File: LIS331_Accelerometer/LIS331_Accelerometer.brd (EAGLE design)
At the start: 39.3 x 26.4 mm, 8 parts, among them U1 LIS331

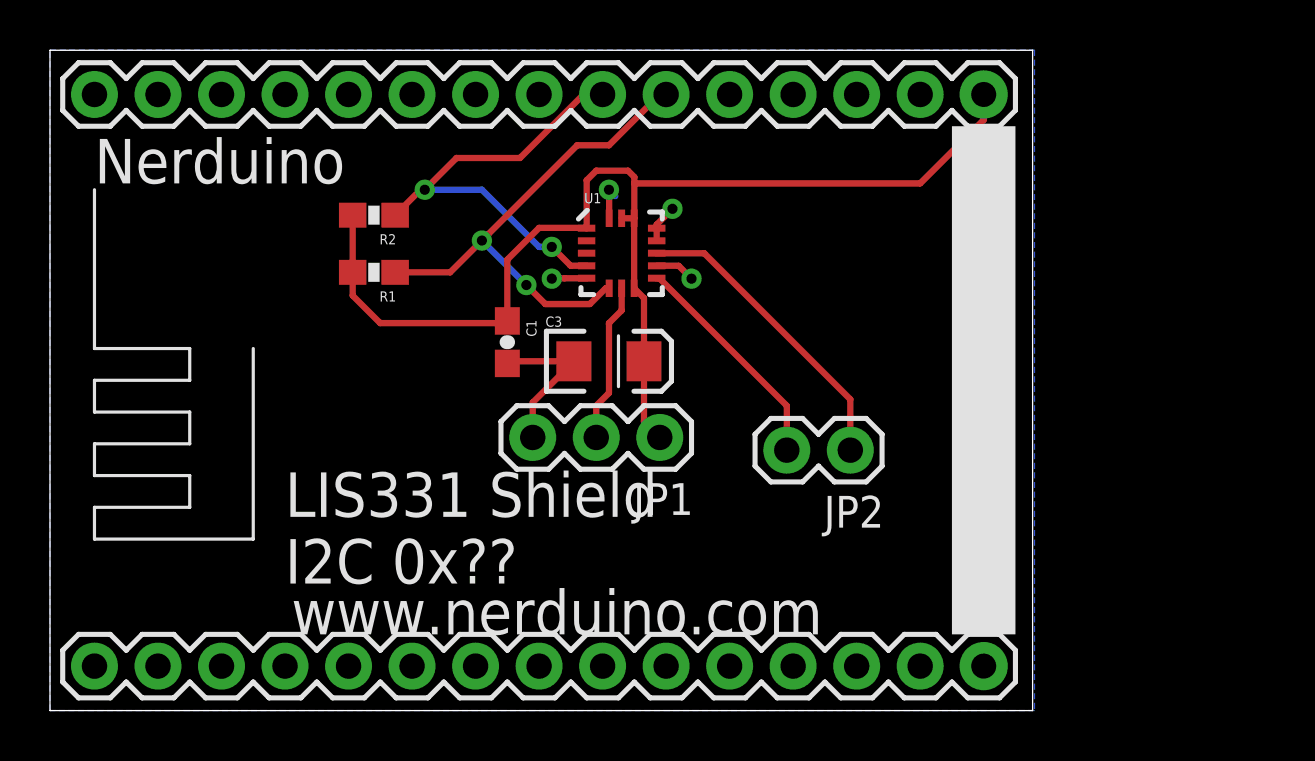
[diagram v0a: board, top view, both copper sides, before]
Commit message: Added OLED Shield Added LiPo Battery Charger Shield Updated outlines of all shields to match the cutout of the nodemcu board
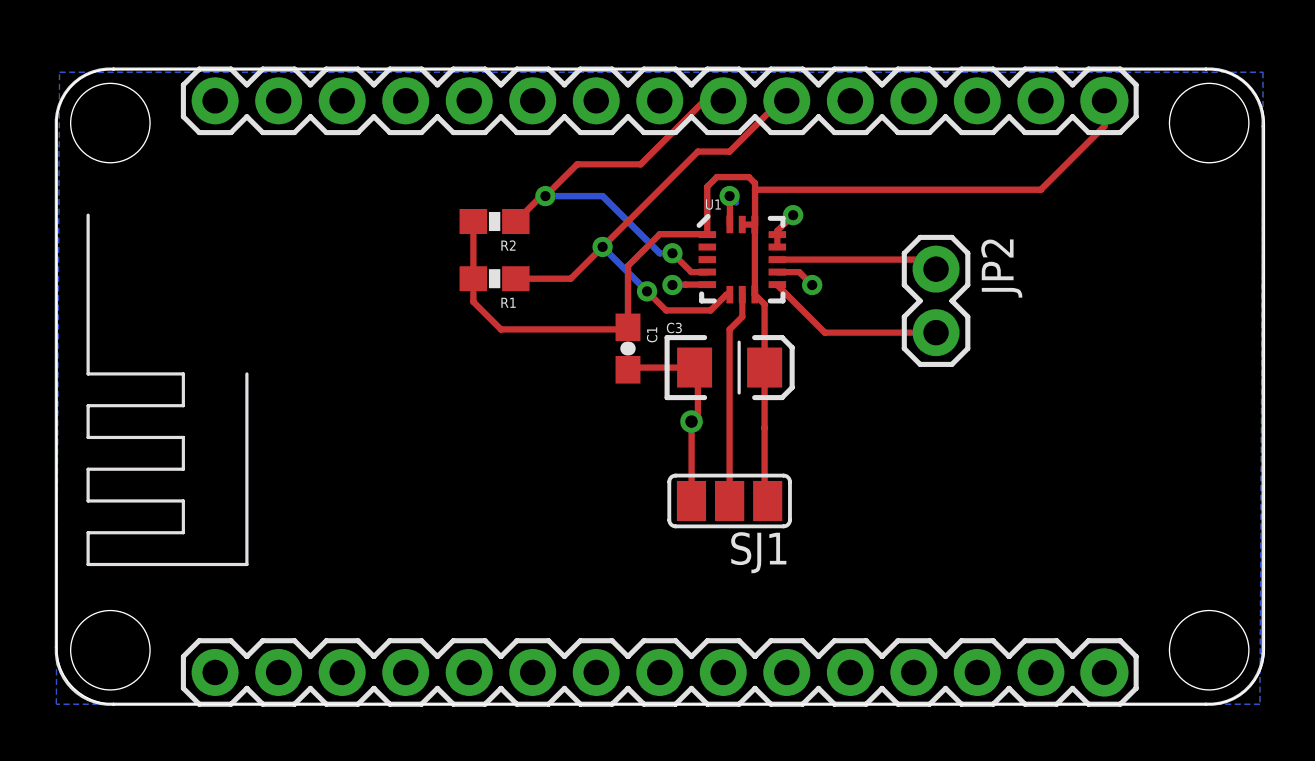
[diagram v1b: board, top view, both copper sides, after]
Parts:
- removed JP1: JP1, SparkFun:1X03
- added SJ1: (no value), SparkFun:SJ_2
- moved JP2 8.01 mm to (35.4, 17.7), turned to 270 degrees
- moved C1 4.83 mm to (23.1, 14.5)
- moved C3 4.83 mm to (27.2, 13.7)
- moved R1 4.83 mm to (17.8, 17.3)
- moved R2 4.83 mm to (17.8, 19.6)
- moved U$2 4.83 mm to (24.4, 6.60)
- moved U1 4.83 mm to (27.7, 18.0)
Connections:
- net +3V3: now also SJ1.1; no longer JP1.1
- net GND: now also SJ1.3; no longer JP1.3, U$2.7
- net N$6: now also SJ1.2; no longer JP1.2
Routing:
- net N$7: track 12.2 -> 6.50 mm
- net +3V3: track 47.6 -> 49.8 mm
- net N$6: track 6.39 -> 8.46 mm
- net N$8: track 9.09 -> 7.15 mm
- net GND: track 13.1 -> 14.9 mm, vias 4 -> 5
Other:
- board size 39.3 x 26.4 mm -> 48.3 x 25.4 mm
- board text added: "NERDUINO LIS331 Shield I2C 0x?? www.nerduino.com"
- board text removed: "LIS331 Shield I2C 0x??"
- board text removed: "Nerduino"
- board text removed: "www.nerduino.com"

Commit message: Updated the i2c pins to all shields to use d11/d12  as these pins will have dual use with the upcoming wifimcu Added FM24W256  Fram shield Added X95840 Digital potentiometer Shield Added AD5696 DAC Shield
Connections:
- net GND: no longer U$2.24
- net N$2: now also U$2.5; no longer U$2.21
- net N$5: now also U$2.4; no longer U$2.22
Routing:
- net N$5: track 18.2 -> 42.1 mm
- net N$2: track 20.5 -> 39.5 mm
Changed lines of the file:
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@@
 <vertex x="0.254" y="0.254"/>
 </polygon>
-<contactref element="U$2" pad="24"/>
 <contactref element="U$2" pad="17"/>
 <contactref element="U$2" pad="14"/>
@@
 <via x="23.876" y="16.764" extent="1-16" drill="0.4064" diameter="0.4064" shape="octagon"/>
 <via x="22.098" y="18.542" extent="1-16" drill="0.4064" diameter="0.4064" shape="octagon"/>
-<contactref element="U$2" pad="21"/>
-<wire x1="29.464" y1="24.384" x2="29.21" y2="24.384" width="0.254" layer="1"/>
 <wire x1="29.21" y1="24.384" x2="27.178" y2="22.352" width="0.254" layer="1"/>
 <wire x1="27.178" y1="22.352" x2="25.908" y2="22.352" width="0.254" layer="1"/>
 <wire x1="25.908" y1="22.352" x2="22.098" y2="18.542" width="0.254" layer="1"/>
+<contactref element="U$2" pad="5"/>
+<wire x1="16.764" y1="1.524" x2="16.764" y2="13.208" width="0.254" layer="16"/>
+<wire x1="16.764" y1="13.208" x2="22.098" y2="18.542" width="0.254" layer="16"/>
 </signal>
 <signal name="N$5">
@@
 <via x="24.892" y="18.288" extent="1-16" drill="0.4064" diameter="0.4064" shape="octagon"/>
 <via x="19.812" y="20.574" extent="1-16" drill="0.4064" diameter="0.4064" shape="octagon"/>
-<contactref element="U$2" pad="22"/>
 <wire x1="19.812" y1="20.574" x2="19.646" y2="20.574" width="0.254" layer="1"/>
-<wire x1="19.646" y1="20.574" x2="18.63" y2="19.558" width="0.254" layer="1"/>
-<wire x1="26.924" y1="24.384" x2="26.162" y2="24.384" width="0.254" layer="1"/>
+<wire x1="19.646" y1="20.574" x2="18.84" y2="19.768" width="0.254" layer="1"/>
+<wire x1="18.84" y1="19.768" x2="18.63" y2="19.558" width="0.254" layer="1"/>
 <wire x1="26.162" y1="24.384" x2="23.622" y2="21.844" width="0.254" layer="1"/>
 <wire x1="23.622" y1="21.844" x2="21.082" y2="21.844" width="0.254" layer="1"/>
 <wire x1="21.082" y1="21.844" x2="19.812" y2="20.574" width="0.254" layer="1"/>
+<contactref element="U$2" pad="4"/>
+<wire x1="14.224" y1="1.524" x2="14.224" y2="19.431" width="0.254" layer="1"/>
+<wire x1="14.224" y1="19.431" x2="16.51" y2="21.717" width="0.254" layer="1"/>
+<wire x1="16.51" y1="21.717" x2="17.653" y2="21.717" width="0.254" layer="1"/>
+<wire x1="17.653" y1="21.717" x2="18.796" y2="20.574" width="0.254" layer="1"/>
+<wire x1="18.796" y1="20.574" x2="18.796" y2="19.812" width="0.254" layer="1"/>
+<wire x1="18.796" y1="19.812" x2="18.84" y2="19.768" width="0.254" layer="1"/>
 </signal>
 <signal name="+3V3">
